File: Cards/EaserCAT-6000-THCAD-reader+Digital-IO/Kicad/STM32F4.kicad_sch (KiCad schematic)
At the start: 25 parts, among them J5 Serial usart1, J7 STLINK, SW1 SW_Push, U6 STM32F407VGT6, Y2 8 MHz

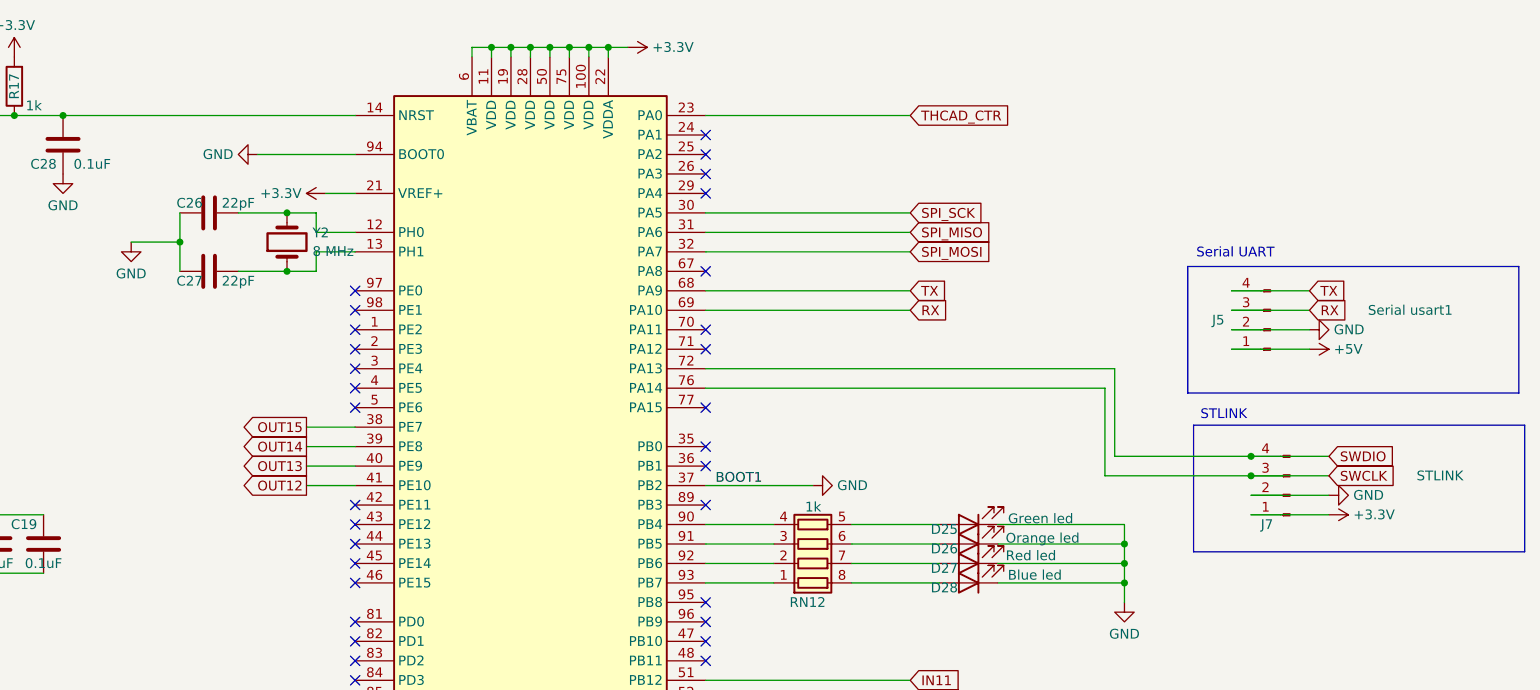
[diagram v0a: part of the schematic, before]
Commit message: Modified, switch marker postions for C28 and R17
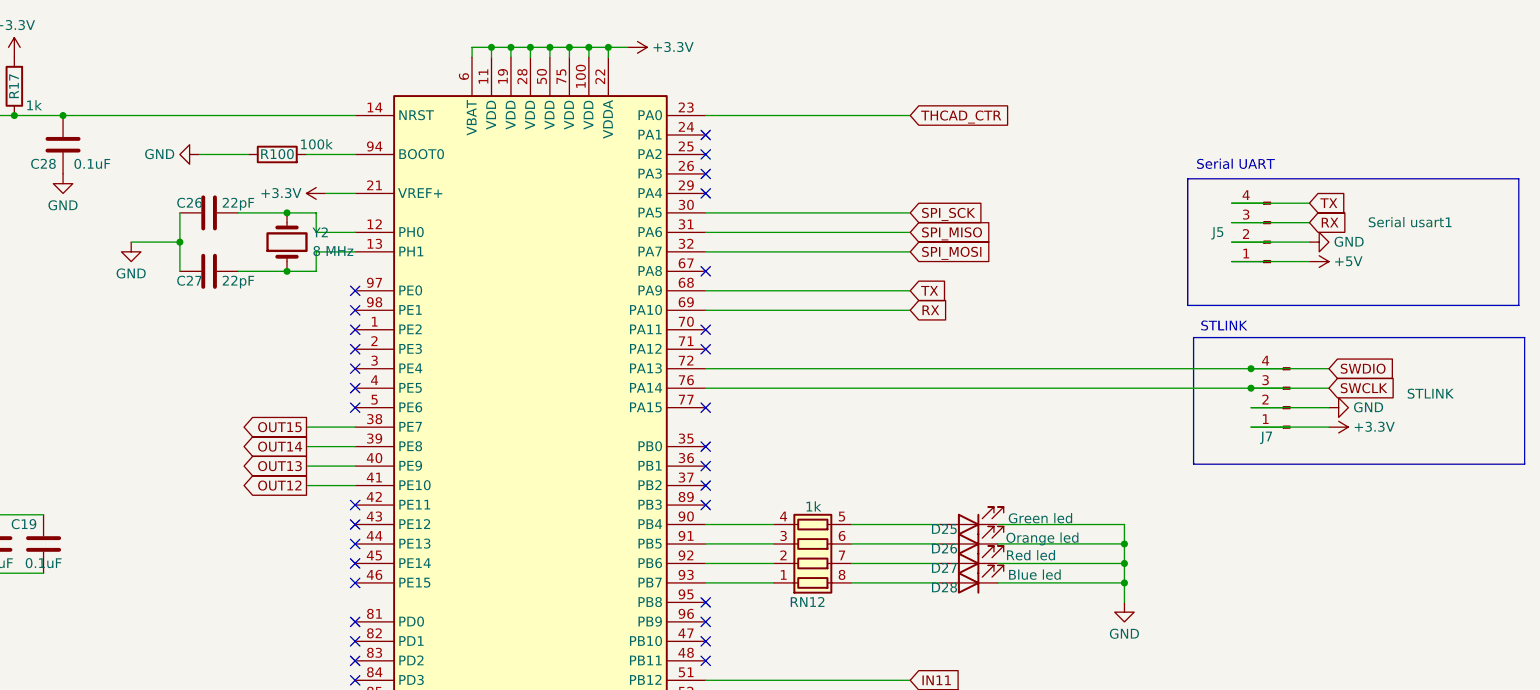
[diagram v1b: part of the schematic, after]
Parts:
- added R100: 100k, Resistor_SMD:R_0603_1608Metric, symbol Device:R
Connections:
- net GND: now also R100.1; no longer U6.37 (PB2), U6.94 (BOOT0)
- new net: R100.2, U6.94 (BOOT0)
- no-connect marks 47 -> 48
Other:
- moved on the sheet: J5, J7
